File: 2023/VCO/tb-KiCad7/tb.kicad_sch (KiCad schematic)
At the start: 2 parts

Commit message: TB もとに戻す。
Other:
- note added: ".include /home/ryos/Project/MakeLSI/MakeLSI.git/2023/VCO/tb-KiCad7/16PTS/mos_PTS06.lib"
- note added: ".tran 1ns 3000ns"
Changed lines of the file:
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@@
     (stroke (width 0) (type default))
+  )
+  (text ".include /home/ryos/Project/MakeLSI/MakeLSI.git/2023/VCO/tb-KiCad7/16PTS/mos_PTS06.lib"
+    (at 100.33 31.75 0)
+    (effects (font (size 1.27 1.27)) (justify left bottom))
+  )
+  (text ".tran 1ns 3000ns\n" (at 101.6 38.1 0)
+    (effects (font (size 1.27 1.27)) (justify left bottom))
   )
   (global_label "VCO_OUT" (shape output) (at 203.2 71.12 0) (fields_autoplaced)
@@
       (effects (font (size 1.27 1.27)) (justify left) hide)
     )
-    (property "Sim.Params" "pwl=\"0 -1 50n -1 51n 0 97n 1 171n -1 200n -1\"" (at 87.63 83.6902 0)
+    (property "Sim.Params" "pwl=\"0 1.2 500n 1.2 1000n 1.4 1500n 1.4 2000n 0.9 2500n 0.9\"" (at 87.63 83.6902 0)
       (effects (font (size 1.27 1.27)) (justify left))
     )

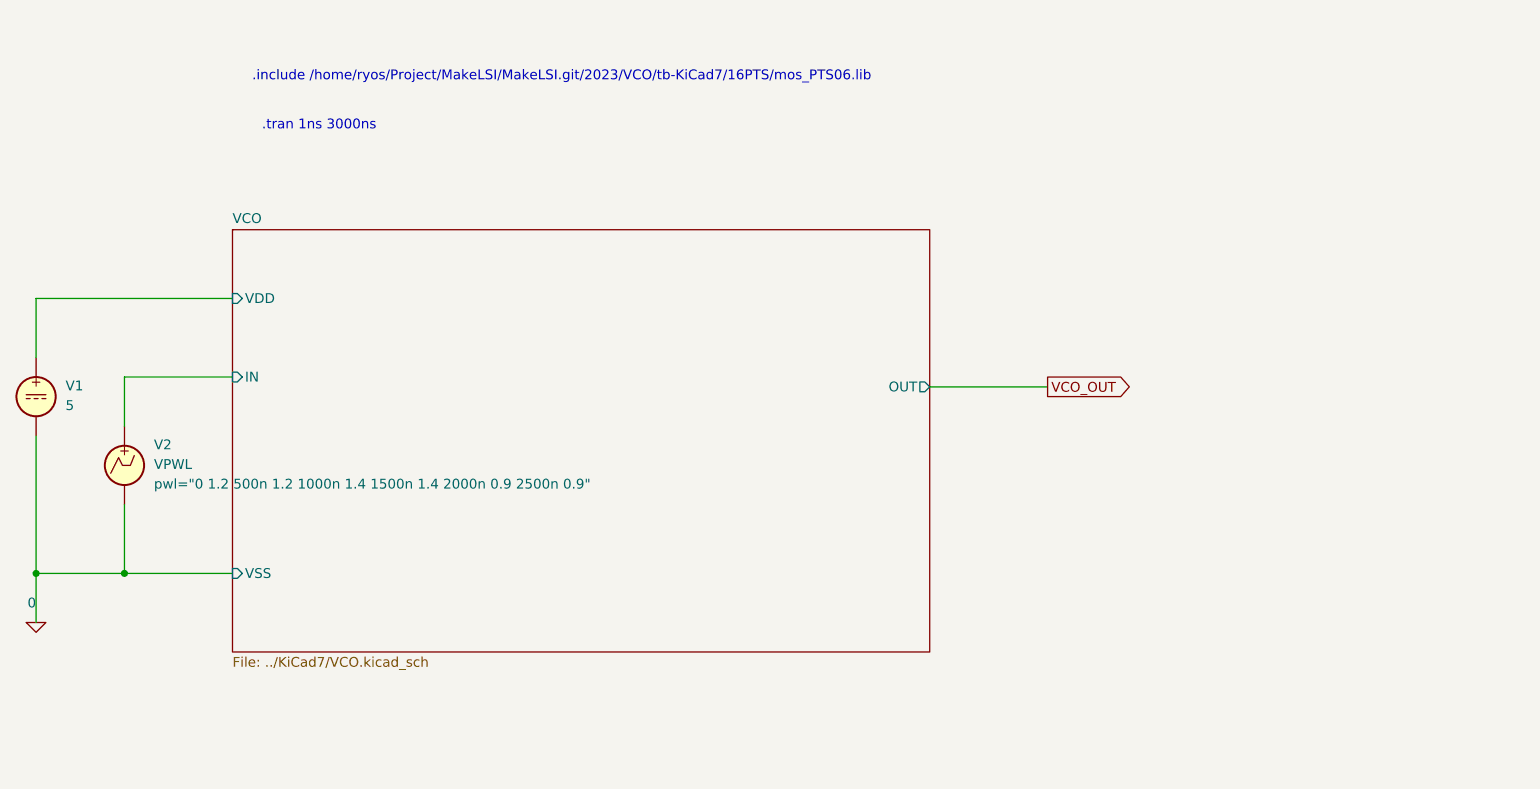
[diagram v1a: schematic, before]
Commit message: 重複しているけど LVS は通った。 バッファ追加前。
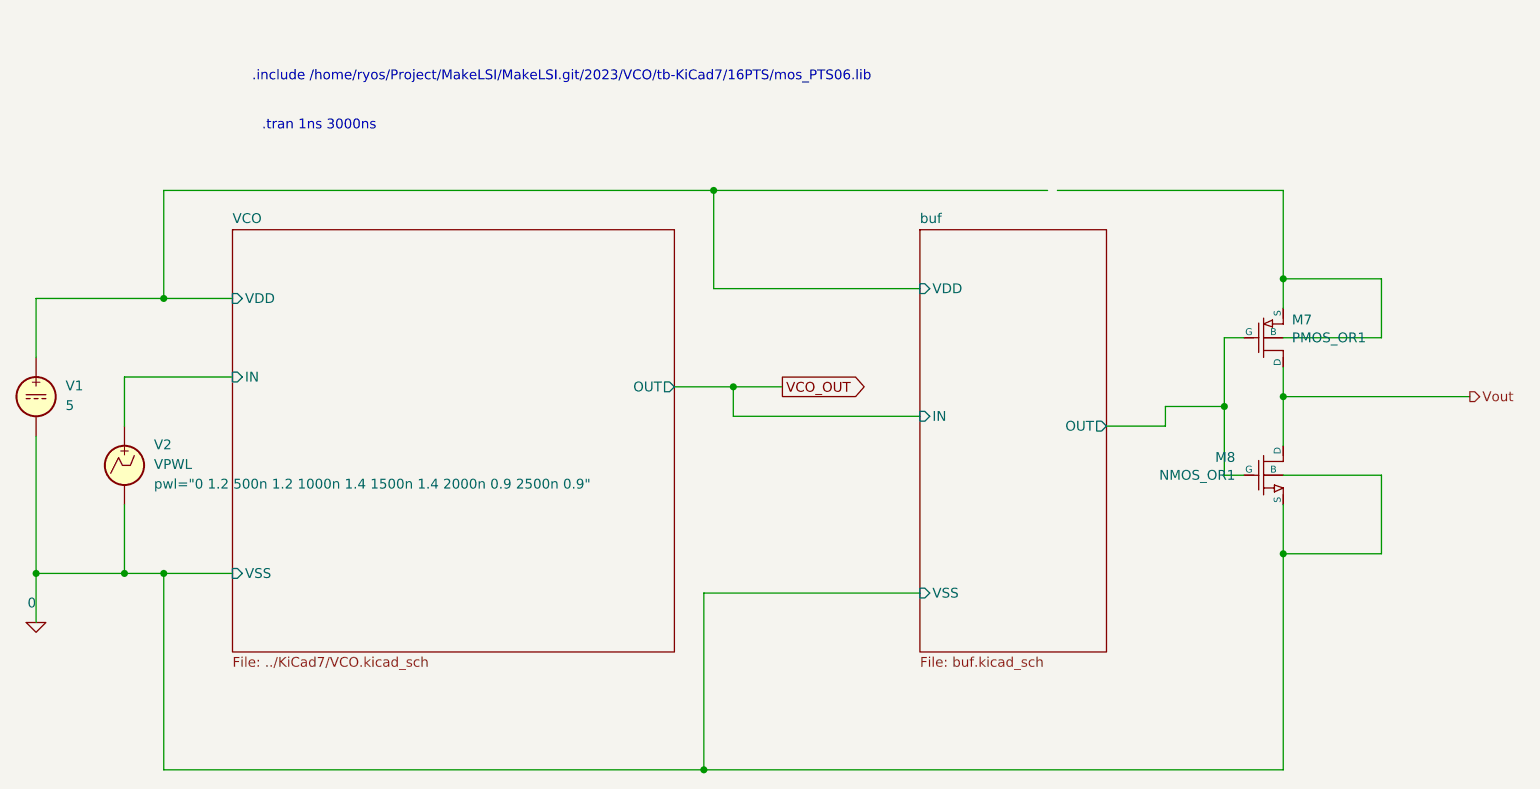
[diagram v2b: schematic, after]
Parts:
- added M7: PMOS_OR1, symbol 0_OR1Symbols:PMOS_OR1
- added M8: NMOS_OR1, symbol 0_OR1Symbols:NMOS_OR1
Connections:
- net 0: now also M8.3 (S), M8.4 (B)
- new net: M7.3 (S), M7.4 (B)
- new net Vout: M7.1 (D), M8.1 (D)
- new net buf/OUT: M7.2 (G), M8.2 (G)
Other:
- added sheet buf (buf.kicad_sch)

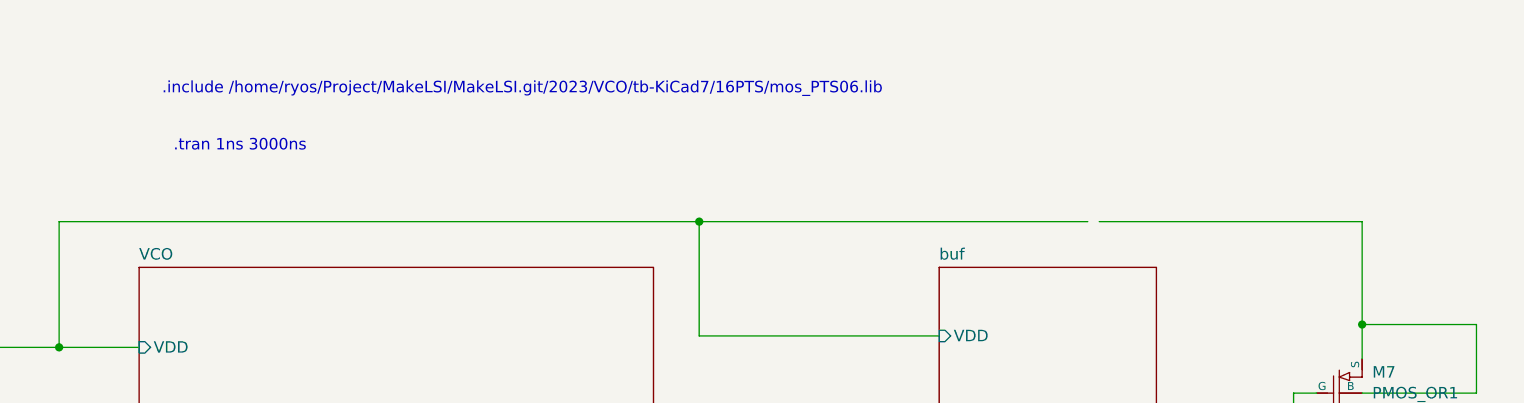
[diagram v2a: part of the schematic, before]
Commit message: VCO_buf のレイアウトが LVS OK.
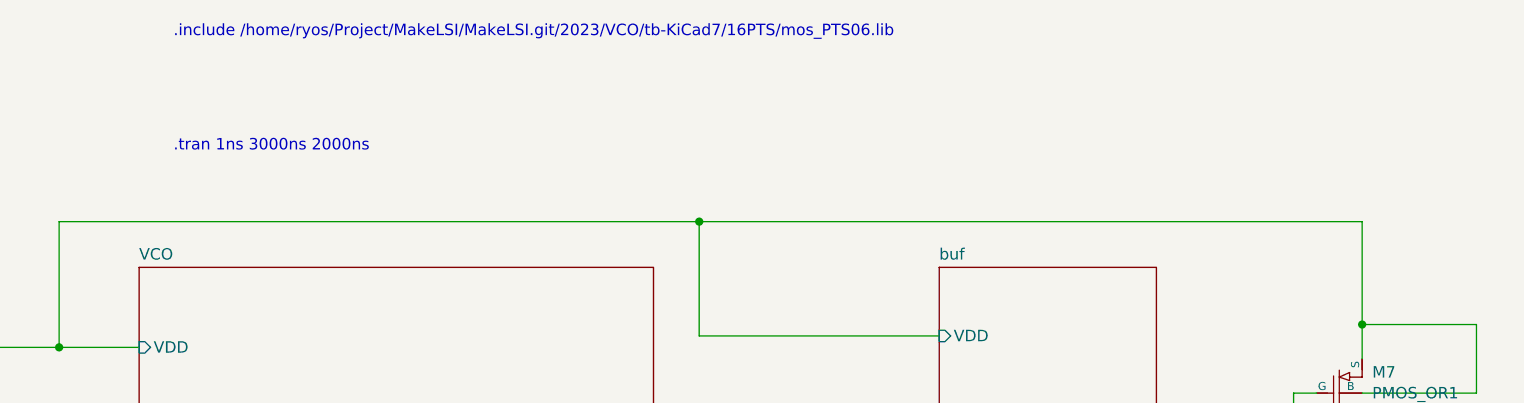
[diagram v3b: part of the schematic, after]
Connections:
- net VCO/VDD: now also M7.3 (S), M7.4 (B)
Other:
- note added: ".tran 1ns 3000ns 2000ns"
- note removed: ".tran 1ns 3000ns"
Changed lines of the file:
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@@
-    (stroke (width 0) (type default))
-  )
-  (wire (pts (xy 204.47 45.72) (xy 233.68 45.72))
     (stroke (width 0) (type default))
   )
@@
     (stroke (width 0) (type default))
   )
-  (wire (pts (xy 160.02 45.72) (xy 203.2 45.72))
+  (wire (pts (xy 160.02 45.72) (xy 233.68 45.72))
     (stroke (width 0) (type default))
   )
@@
   )
   (text ".include /home/ryos/Project/MakeLSI/MakeLSI.git/2023/VCO/tb-KiCad7/16PTS/mos_PTS06.lib"
-    (at 100.33 31.75 0)
+    (at 101.6 25.4 0)
     (effects (font (size 1.27 1.27)) (justify left bottom))
   )
-  (text ".tran 1ns 3000ns\n" (at 101.6 38.1 0)
+  (text ".tran 1ns 3000ns 2000ns\n" (at 101.6 38.1 0)
     (effects (font (size 1.27 1.27)) (justify left bottom))
   )
